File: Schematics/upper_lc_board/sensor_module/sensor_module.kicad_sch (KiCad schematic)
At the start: 54 parts, among them J2 HAL_SENS, J3 PT1, J4 PT2, J7 TC, U10 OA-TLV9001IDCK, U11 OA-TLV9001IDCK, U12 OA-TLV9001IDCK, U5 TMP117MAIDRVR, U7 ADC_ADS131M04IPWR, U9 OA-TLV9001IDCK

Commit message: temp commit for layout work
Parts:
- C30, C31: footprint (none) -> Capacitor_SMD:C_0603_1608Metric
- R16, R17, R18, R19, R27, R42, R43, R44, R45: footprint (none) -> Resistor_SMD:R_0402_1005Metric
- R28, R29, R30, R31, R32, R33, R34, R35, R36, R37, R38, R39: footprint Capacitor_SMD:C_0402_1005Metric -> Resistor_SMD:R_0402_1005Metric
- R46, R47: footprint (none) -> Resistor_SMD:R_0603_1608Metric
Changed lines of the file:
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@@
 			)
 		)
-		(property "Footprint" "Capacitor_SMD:C_0402_1005Metric"
+		(property "Footprint" "Resistor_SMD:R_0402_1005Metric"
 			(at 135.89 83.058 90)
 			(effects
@@
 			)
 		)
-		(property "Footprint" ""
+		(property "Footprint" "Resistor_SMD:R_0402_1005Metric"
 			(at 61.722 146.05 90)
 			(effects
@@
 			)
 		)
-		(property "Footprint" "Capacitor_SMD:C_0402_1005Metric"
+		(property "Footprint" "Resistor_SMD:R_0402_1005Metric"
 			(at 135.89 70.358 90)
 			(effects
@@
 			)
 		)
-		(property "Footprint" ""
+		(property "Footprint" "Resistor_SMD:R_0402_1005Metric"
 			(at 273.558 140.97 90)
 			(effects
@@
 			)
 		)
-		(property "Footprint" "Capacitor_SMD:C_0402_1005Metric"
+		(property "Footprint" "Resistor_SMD:R_0402_1005Metric"
 			(at 135.89 75.438 90)
 			(effects
@@
 			)
 		)
-		(property "Footprint" ""
+		(property "Footprint" "Resistor_SMD:R_0402_1005Metric"
 			(at 273.558 154.94 90)
 			(effects
@@
 			)
 		)
-		(property "Footprint" ""
+		(property "Footprint" "Resistor_SMD:R_0402_1005Metric"
 			(at 113.792 163.83 90)
 			(effects
@@
 			)
 		)
-		(property "Footprint" ""
+		(property "Footprint" "Capacitor_SMD:C_0603_1608Metric"
 			(at 229.87 157.1752 0)
 			(effects
@@
 			)
 		)
-		(property "Footprint" ""
+		(property "Footprint" "Resistor_SMD:R_0402_1005Metric"
 			(at 61.722 158.75 90)
 			(effects
@@
 			)
 		)
-		(property "Footprint" "Capacitor_SMD:C_0402_1005Metric"
+		(property "Footprint" "Resistor_SMD:R_0402_1005Metric"
 			(at 239.522 95.25 90)
 			(effects
@@
 			)
 		)
-		(property "Footprint" "Capacitor_SMD:C_0402_1005Metric"
+		(property "Footprint" "Resistor_SMD:R_0402_1005Metric"
 			(at 135.89 94.488 90)
 			(effects
@@
 			)
 		)
-		(property "Footprint" ""
+		(property "Footprint" "Resistor_SMD:R_0402_1005Metric"
 			(at 48.26 72.898 90)
 			(effects
@@
 			)
 		)
-		(property "Footprint" ""
+		(property "Footprint" "Resistor_SMD:R_0402_1005Metric"
 			(at 132.842 165.1 90)
 			(effects
@@
 			)
 		)
-		(property "Footprint" "Capacitor_SMD:C_0402_1005Metric"
+		(property "Footprint" "Resistor_SMD:R_0402_1005Metric"
 			(at 261.112 95.25 90)
 			(effects
@@
 			)
 		)
-		(property "Footprint" ""
+		(property "Footprint" "Capacitor_SMD:C_0603_1608Metric"
 			(at 259.3848 139.7 0)
 			(effects
@@
 			)
 		)
-		(property "Footprint" ""
+		(property "Footprint" "Resistor_SMD:R_0402_1005Metric"
 			(at 150.622 165.1 90)
 			(effects
@@
 			)
 		)
-		(property "Footprint" ""
+		(property "Footprint" "Resistor_SMD:R_0603_1608Metric"
 			(at 184.912 151.13 90)
 			(effects
@@
 			)
 		)
-		(property "Footprint" "Capacitor_SMD:C_0402_1005Metric"
+		(property "Footprint" "Resistor_SMD:R_0402_1005Metric"
 			(at 228.092 95.25 90)
 			(effects
@@
 			)
 		)
-		(property "Footprint" "Capacitor_SMD:C_0402_1005Metric"
+		(property "Footprint" "Resistor_SMD:R_0402_1005Metric"
 			(at 135.89 58.928 90)
 			(effects
@@
 			)
 		)
-		(property "Footprint" "Capacitor_SMD:C_0402_1005Metric"
+		(property "Footprint" "Resistor_SMD:R_0402_1005Metric"
 			(at 250.952 95.25 90)
 			(effects
@@
 			)
 		)
-		(property "Footprint" "Capacitor_SMD:C_0402_1005Metric"
+		(property "Footprint" "Resistor_SMD:R_0402_1005Metric"
 			(at 135.89 62.738 90)
 			(effects
@@
 			)
 		)
-		(property "Footprint" "Capacitor_SMD:C_0402_1005Metric"
+		(property "Footprint" "Resistor_SMD:R_0402_1005Metric"
 			(at 135.89 86.868 90)
 			(effects
@@
 			)
 		)
-		(property "Footprint" ""
+		(property "Footprint" "Resistor_SMD:R_0603_1608Metric"
 			(at 184.912 135.89 90)
 			(effects
@@
 			)
 		)
-		(property "Footprint" "Capacitor_SMD:C_0402_1005Metric"
+		(property "Footprint" "Resistor_SMD:R_0402_1005Metric"
 			(at 135.89 51.308 90)
 			(effects
@@
 			)
 		)
-		(property "Footprint" ""
+		(property "Footprint" "Resistor_SMD:R_0402_1005Metric"
 			(at 48.26 112.268 90)
 			(effects

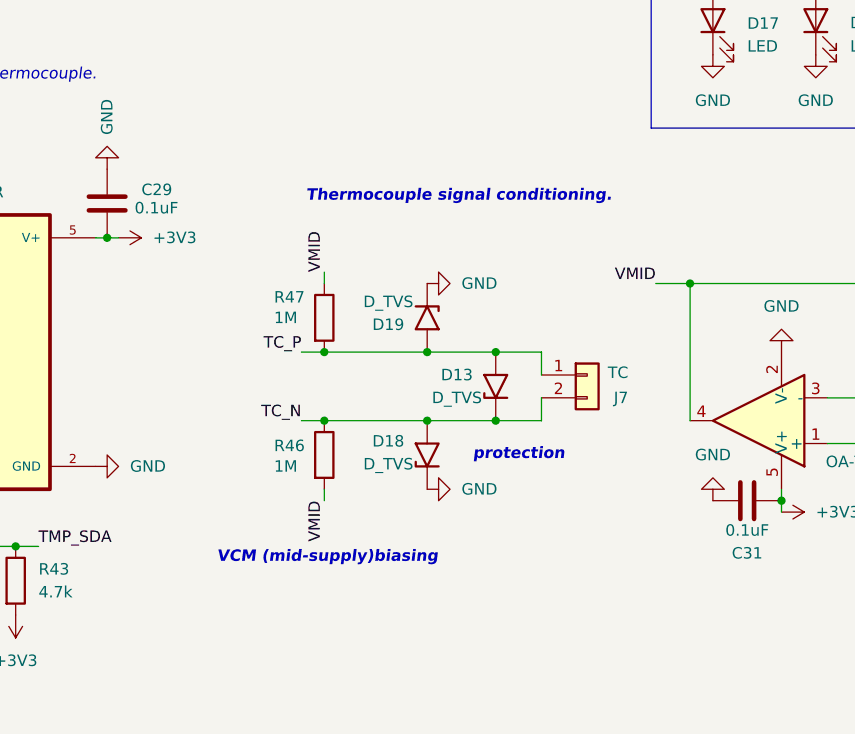
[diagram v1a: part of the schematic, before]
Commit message: update schematic & board with smaller diode footprints
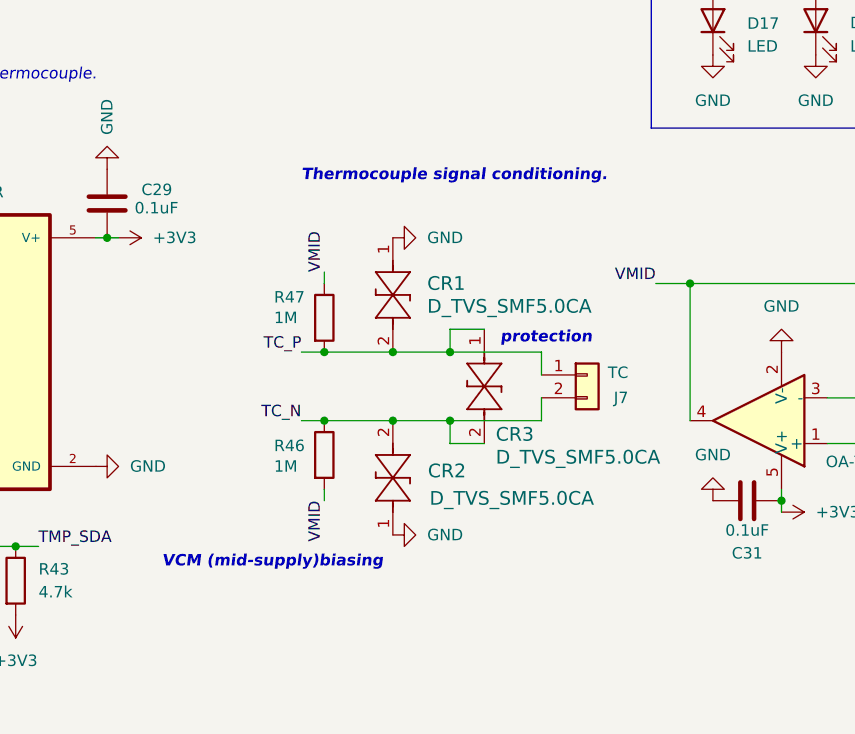
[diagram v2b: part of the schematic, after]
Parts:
- removed D13, D18, D19: D_TVS, SMBJ28A:DIOM5436X244N, symbol Diode:1.5KExxA
- added CR1, CR2, CR3: D_TVS_SMF5.0CA, SMF5_0CA:SOD-123F_LTF-L, symbol TVS-SMF:SMF5.0CA
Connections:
- net GND: now also CR1.1, CR2.1
- net TC_N: now also CR2.2, CR3.2
- net TC_P: now also CR1.2, CR3.1

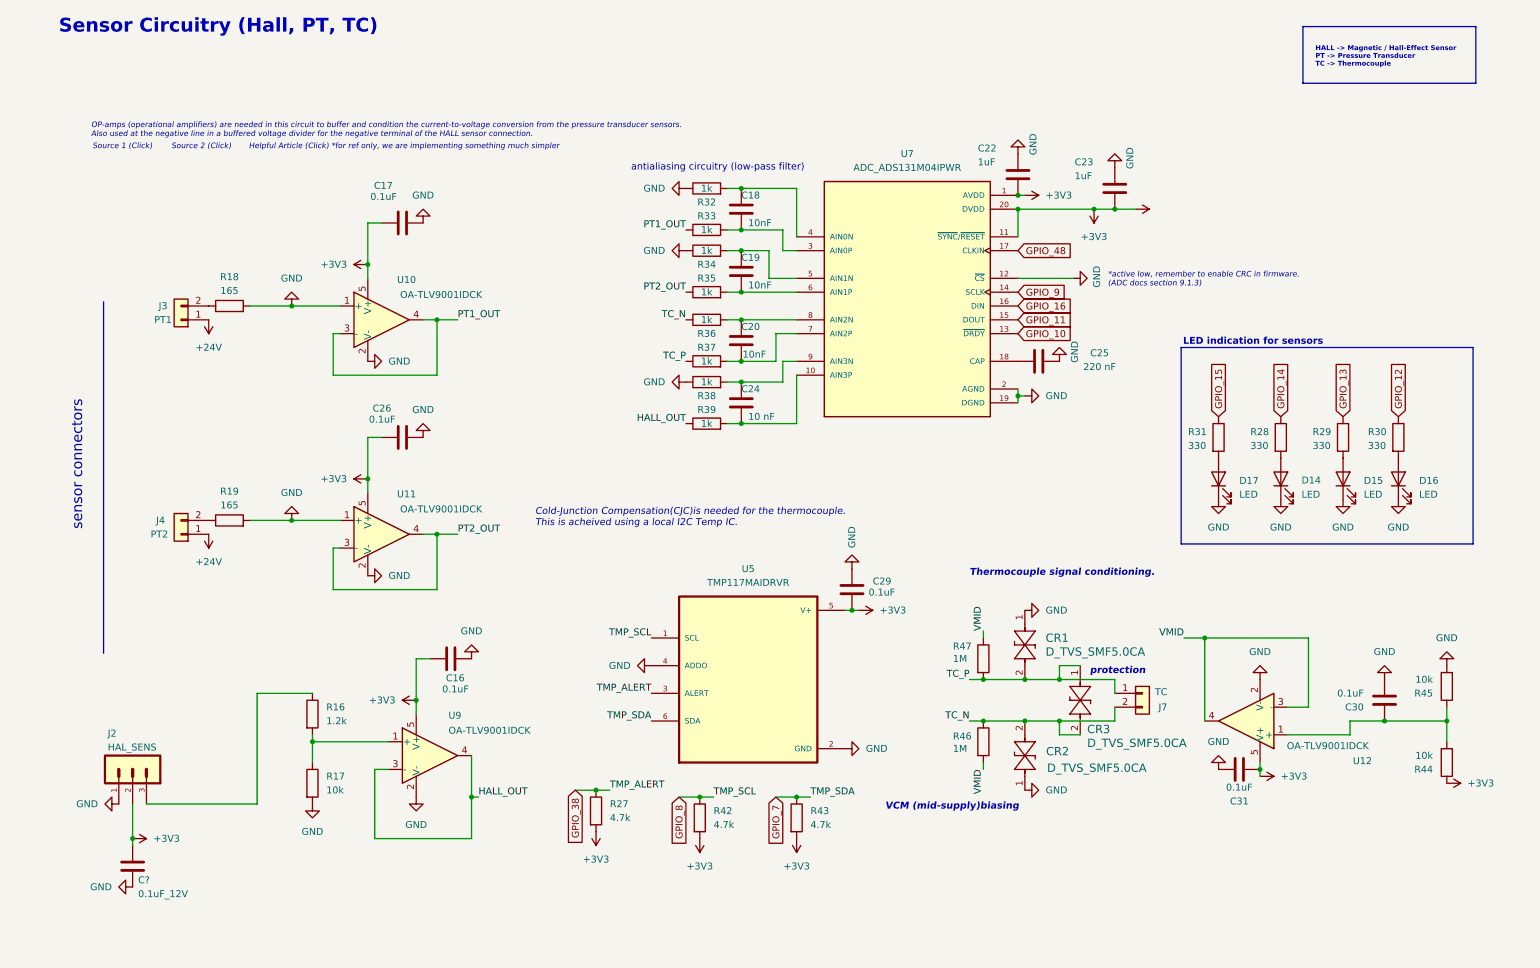
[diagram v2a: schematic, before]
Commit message: revise & organize some circuitry, next: replace MUX with ideal diodes, finish layout, rename GPIO labels for clarity
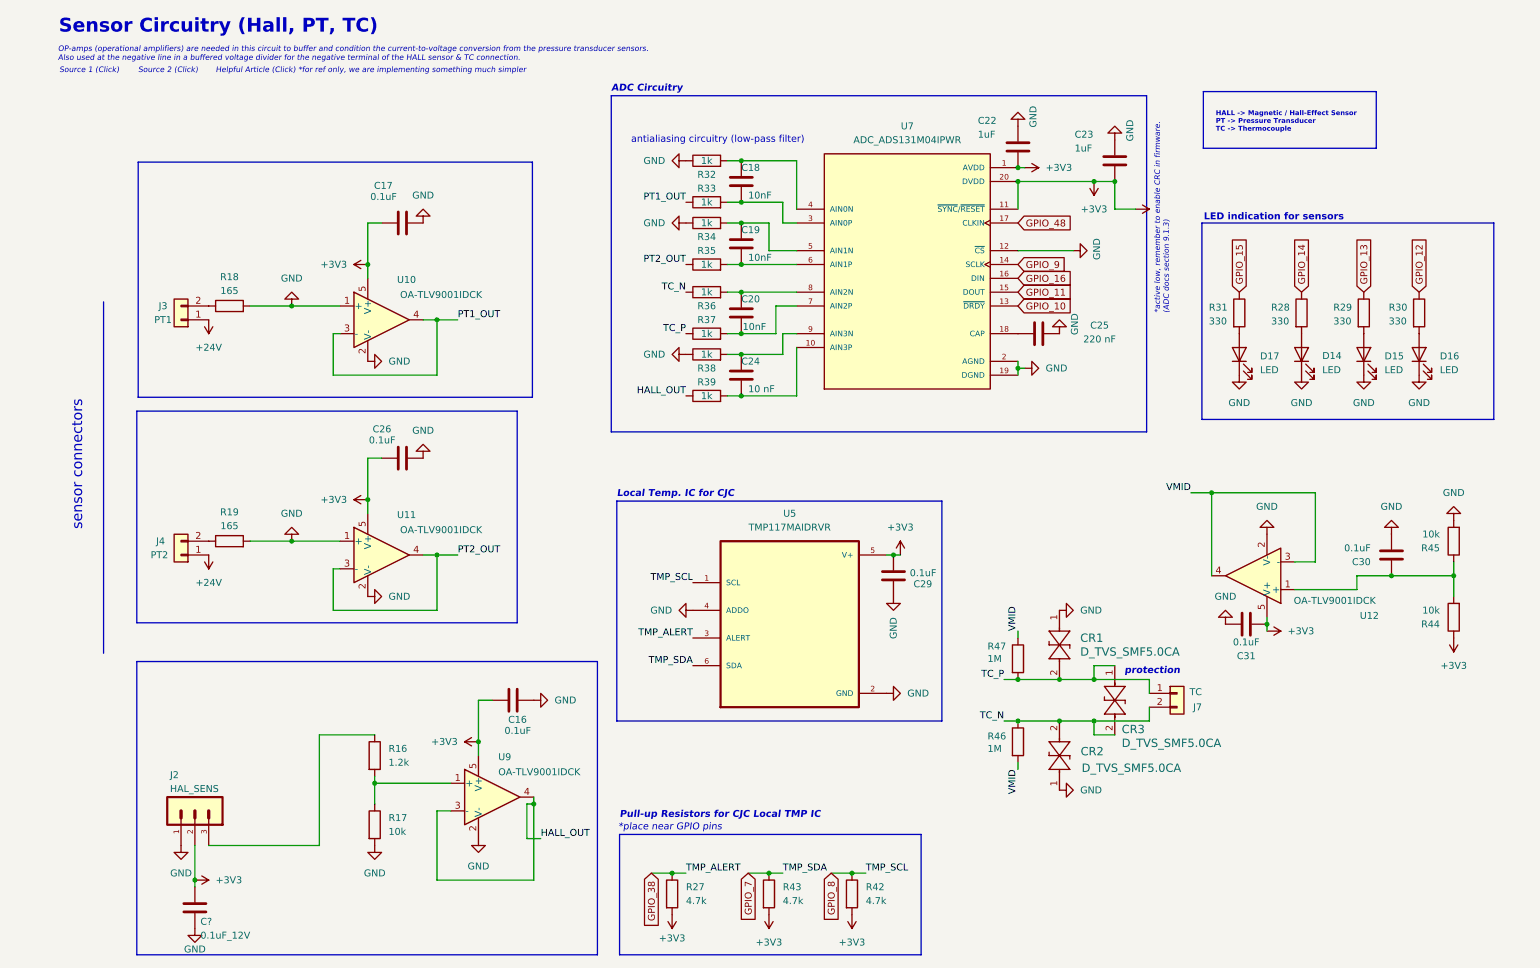
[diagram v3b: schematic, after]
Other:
- note added: "*place near GPIO pins"
- note added: "ADC Circuitry"
- note added: "Local Temp. IC for CJC"
- note added: "OP-amps (operational amplifiers) are needed in this circuit to buffer and condition the current-to-voltage conversion from the pressure transducer sensors. Also used at the negative line in a buffered voltage divider for the negative terminal of the HALL sensor & TC connection."
- note added: "Pull-up Resistors for CJC Local TMP IC"
- note removed: "Cold-Junction Compensation(CJC)is needed for the thermocouple. This is acheived using a local I2C Temp IC."
- note removed: "OP-amps (operational amplifiers) are needed in this circuit to buffer and condition the current-to-voltage conversion from the pressure transducer sensors. Also used at the negative line in a buffered voltage divider for the negative terminal of the HALL sensor connection."
- note removed: "Thermocouple signal conditioning."
- note removed: "VCM (mid-supply)biasing"
- moved on the sheet: C16, C18, C19, C20, C22, C23, C24, C25, C26, C29, C30, C31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

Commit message: more layout work, add FAULT LED
next: revert to ideal diode circuitry instead of MUX IC.
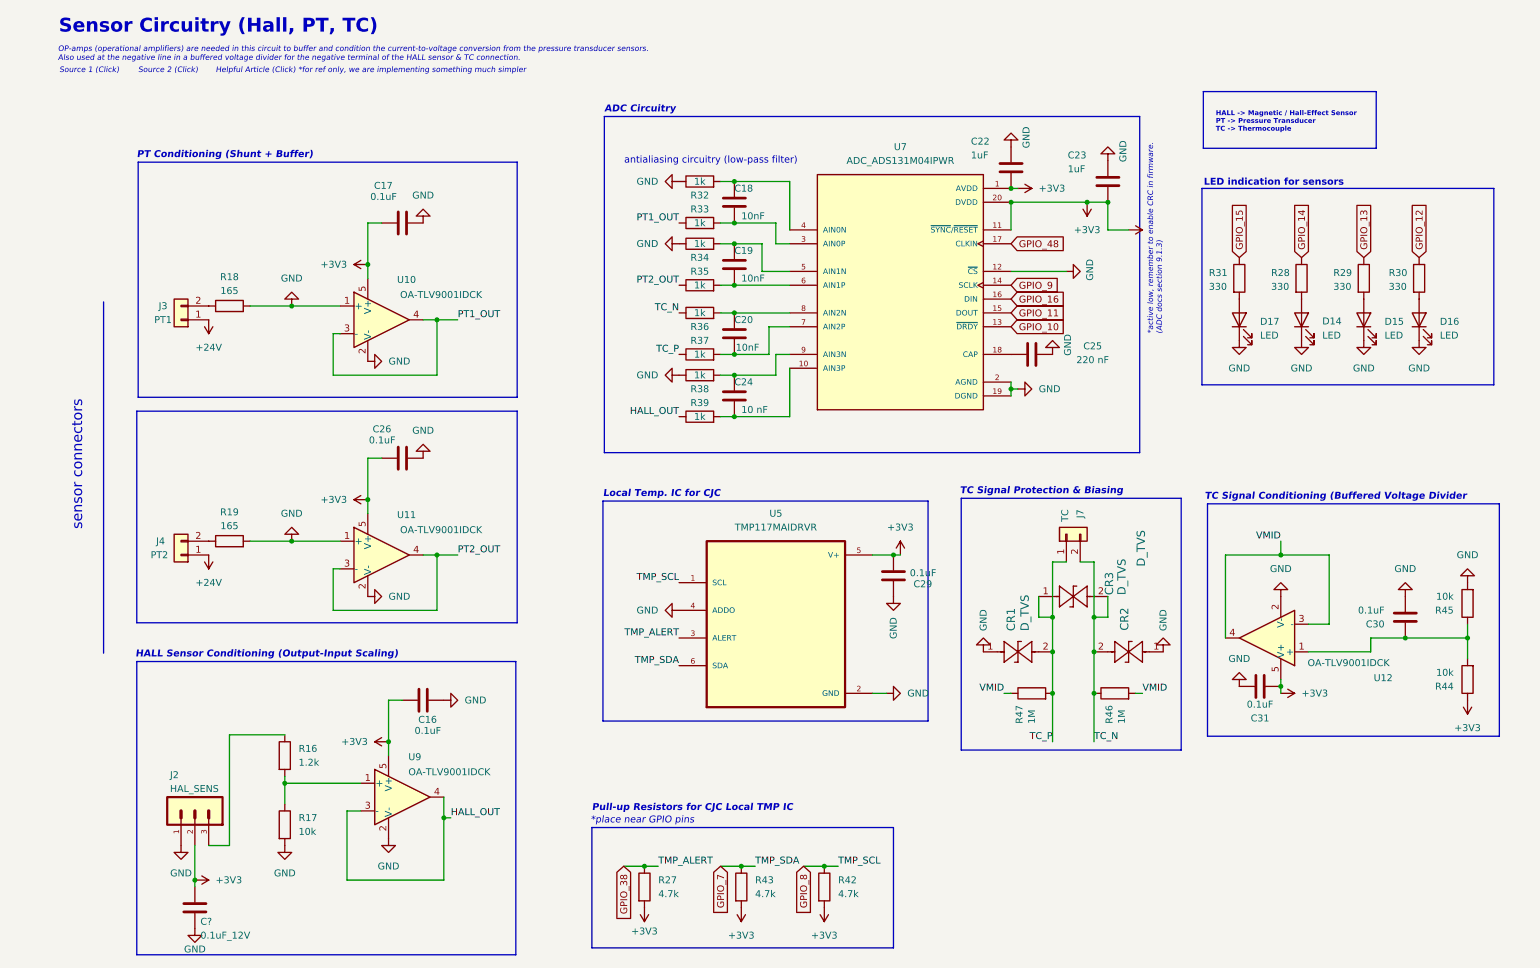
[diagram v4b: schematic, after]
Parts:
- CR1, CR2, CR3: value D_TVS_SMF5.0CA -> D_TVS
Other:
- note added: "HALL Sensor Conditioning (Output-Input Scaling)"
- note added: "PT Conditioning (Shunt + Buffer)"
- note added: "TC Signal Conditioning (Buffered Voltage Divider"
- note added: "TC Signal Protection & Biasing"
- note removed: "protection"
- moved on the sheet: C16, C18, C19, C20, C22, C23, C24, C25, C30, C31, CR1, CR2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

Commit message: add vertical connectors, revert MUX circuitry to ORing setup w ideal diodes
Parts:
- J3, J4: footprint 530480210:MOLEX_530480210 -> CONNS:CONN02_530470260_MOL
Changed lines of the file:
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@@
 			)
 		)
-		(property "Footprint" "530480210:MOLEX_530480210"
+		(property "Footprint" "CONNS:CONN02_530470260_MOL"
 			(at 39.37 116.84 0)
 			(effects
@@
 			)
 		)
-		(property "Footprint" "530480210:MOLEX_530480210"
+		(property "Footprint" "CONNS:CONN02_530470260_MOL"
 			(at 39.37 73.66 0)
 			(effects
